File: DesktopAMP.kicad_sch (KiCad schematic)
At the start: 73 parts, among them J1 Conn_02x20_Odd_Even, J2 Conn_02x01, J3 Conn_01x03, J4 Conn_01x04, J5 Conn_01x03, Q1 DMG2305UX, U1 LM1117-3.3, U2 LM2592HV, U3 LM1117-3.3, U4 DMMT5401, U5 PCM5242, U6 AT24CS01-STUM, U7 LM4780, X1 22.5792MHz, X2 24.5760MHz

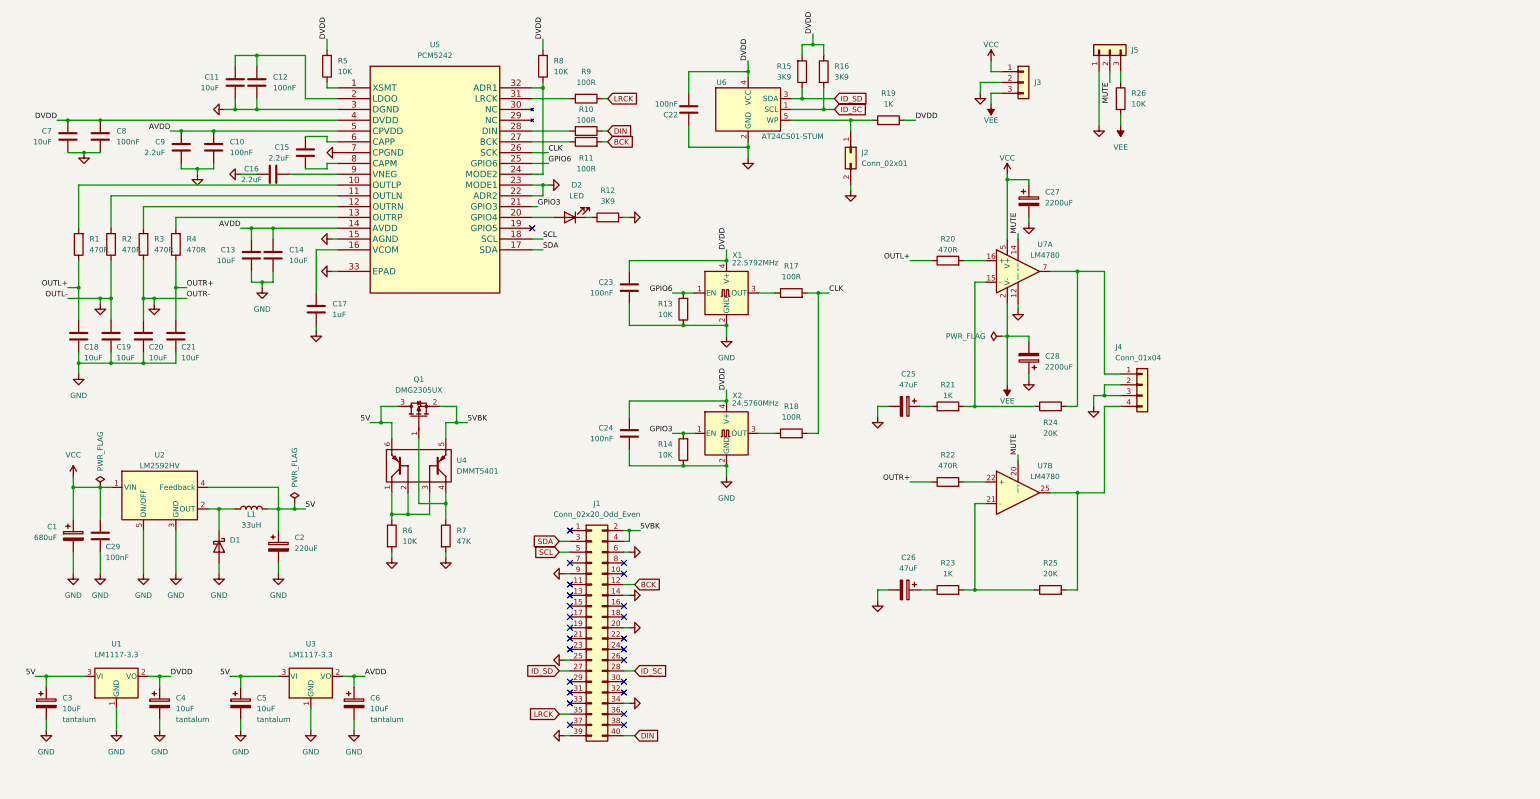
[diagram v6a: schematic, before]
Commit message: Begun splitting schematic into multiple sheets.
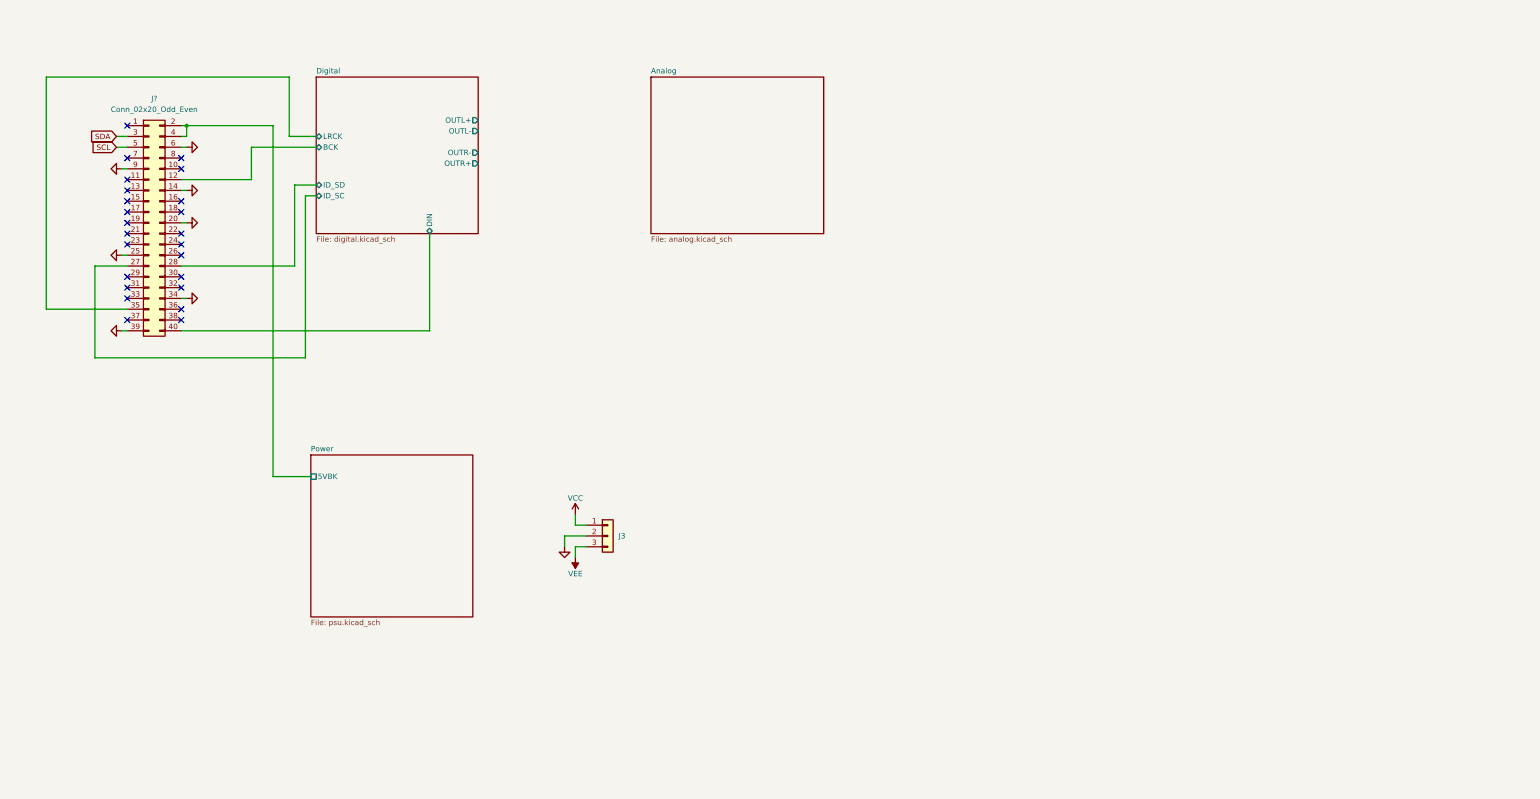
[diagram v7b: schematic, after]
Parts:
- removed C1: 680uF, Capacitor_THT:CP_Radial_D10.0mm_P3.50mm, symbol Device:C_Polarized
- removed C10, C12, C22, C23, C24, C29, C8: 100nF, Capacitor_SMD:C_0805_2012Metric, symbol Device:C
- removed C11, C13, C14, C18, C19, C20, C21, C7: 10uF, Capacitor_SMD:C_0805_2012Metric, symbol Device:C
- removed C15, C16, C9: 2.2uF, Capacitor_SMD:C_0805_2012Metric, symbol Device:C
- removed C17: 1uF, Capacitor_SMD:C_0805_2012Metric, symbol Device:C
- removed C2: 220uF, Capacitor_THT:CP_Radial_D8.0mm_P3.50mm, symbol Device:C_Polarized
- removed C25, C26: 47uF, Capacitor_THT:CP_Radial_D6.3mm_P2.50mm, symbol Device:C_Polarized
- removed C27, C28: 2200uF, Capacitor_THT:CP_Radial_D18.0mm_P7.50mm, symbol Device:C_Polarized
- removed C3, C4, C5, C6: 10uF, Capacitor_SMD:C_0805_2012Metric, symbol Device:C_Polarized
- removed D1: SSC54-E3/9AT, Diode_SMD:D_SMC, symbol Diode:1N5822
- removed D2: LED, Resistor_SMD:R_0805_2012Metric, symbol Device:LED
- removed J1: Conn_02x20_Odd_Even, Etnolit:RPi_Zero_2W, symbol Connector_Generic:Conn_02x20_Odd_Even
- removed J2: Conn_02x01, Resistor_SMD:R_0805_2012Metric, symbol Connector_Generic:Conn_02x01
- removed J4: Conn_01x04, Connector_Phoenix_MSTB:PhoenixContact_MSTBVA_2,5_4-G_1x04_P5.00mm_Vertical, symbol Connector_Generic:Conn_01x04
- removed J5: Conn_01x03, Connector_PinHeader_2.54mm:PinHeader_1x03_P2.54mm_Vertical, symbol Connector_Generic:Conn_01x03
- removed L1: 33uH, Inductor_SMD:L_Bourns_SRR1260, symbol Device:L
- removed Q1: DMG2305UX, Package_TO_SOT_SMD:SOT-23, symbol Etnolit:DMG2305UX
- removed R1, R2, R20, R22, R3, R4: 470R, Resistor_SMD:R_0805_2012Metric, symbol Device:R
- removed R10, R11, R17, R18, R9: 100R, Resistor_SMD:R_0805_2012Metric, symbol Device:R
- removed R12, R15, R16: 3K9, Resistor_SMD:R_0805_2012Metric, symbol Device:R
- removed R13, R14, R26, R5, R6, R8: 10K, Resistor_SMD:R_0805_2012Metric, symbol Device:R
- removed R19, R21, R23: 1K, Resistor_SMD:R_0805_2012Metric, symbol Device:R
- removed R24, R25: 20K, Resistor_SMD:R_0805_2012Metric, symbol Device:R
- removed R7: 47K, Resistor_SMD:R_0805_2012Metric, symbol Device:R
- removed U1, U3: LM1117-3.3, Package_TO_SOT_SMD:SOT-223-3_TabPin2, symbol Regulator_Linear:LM1117-3.3
- removed U2: LM2592HV, Package_TO_SOT_SMD:TO-263-5_TabPin3, symbol Etnolit:LM2592HV
- removed U4: DMMT5401, Package_TO_SOT_SMD:SOT-23-6, symbol Etnolit:DMMT5401
- removed U5: PCM5242, Package_DFN_QFN:Texas_S-PVQFN-N32_EP3.45x3.45mm_ThermalVias, symbol Etnolit:PCM5242RHB
- removed U6: AT24CS01-STUM, Package_TO_SOT_SMD:SOT-23-5, symbol Memory_EEPROM:AT24CS01-STUM
- removed U7: LM4780, Etnolit:TO-220-27, symbol Etnolit:LM4780
- removed X1: 22.5792MHz, Oscillator:Oscillator_SMD_EuroQuartz_XO53-4Pin_5.0x3.2mm, symbol Oscillator:XO53
- removed X2: 24.5760MHz, Oscillator:Oscillator_SMD_EuroQuartz_XO53-4Pin_5.0x3.2mm, symbol Oscillator:XO53
- added J?: Conn_02x20_Odd_Even, Etnolit:RPi_Zero_2W, symbol Connector_Generic:Conn_02x20_Odd_Even
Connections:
- net GND: now also J?.14 (Pin_14), J?.20 (Pin_20), J?.25 (Pin_25), J?.34 (Pin_34), J?.39 (Pin_39), J?.6 (Pin_6), J?.9 (Pin_9)
- net SCL: now also J?.5 (Pin_5)
- net SDA: now also J?.3 (Pin_3)
- new net Digital/BCK: J?.12 (Pin_12)
- new net Digital/DIN: J?.40 (Pin_40)
- new net Digital/ID_SC: J?.27 (Pin_27)
- new net Digital/ID_SD: J?.28 (Pin_28)
- new net Digital/LRCK: J?.35 (Pin_35)
- new net Power/5VBK: J?.2 (Pin_2), J?.4 (Pin_4)
- no-connect marks 25 -> 24
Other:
- added sheet Analog (analog.kicad_sch)
- added sheet Digital (digital.kicad_sch)
- added sheet Power (psu.kicad_sch)
- moved on the sheet: J3

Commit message: WIP
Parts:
- gave numbers to parts that had none: 1
- renumbered J3 to J2
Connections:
- net SCL renamed Digital/SCL
- net SDA renamed Digital/SDA
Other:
- sheet Analog ports: added OUTL+, OUTL-, OUTR+, OUTR-; removed none
- sheet Digital ports: added SCL, SDA; removed none
